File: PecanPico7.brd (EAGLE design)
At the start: 34.2 x 50 mm, 172 parts, among them IC1 Si4464-B1B-FM, IC13 RF6886, IC15 MPU-9250, IC16 PAC1720-1-AIA-TR, IC2 Si4464-B1B-FM, IC3 BME280_BME280, IC4 UBLOX_MAX-6, IC5 STM32F429IIH6, IC6 ALM-GP003, IC7 SPV1040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

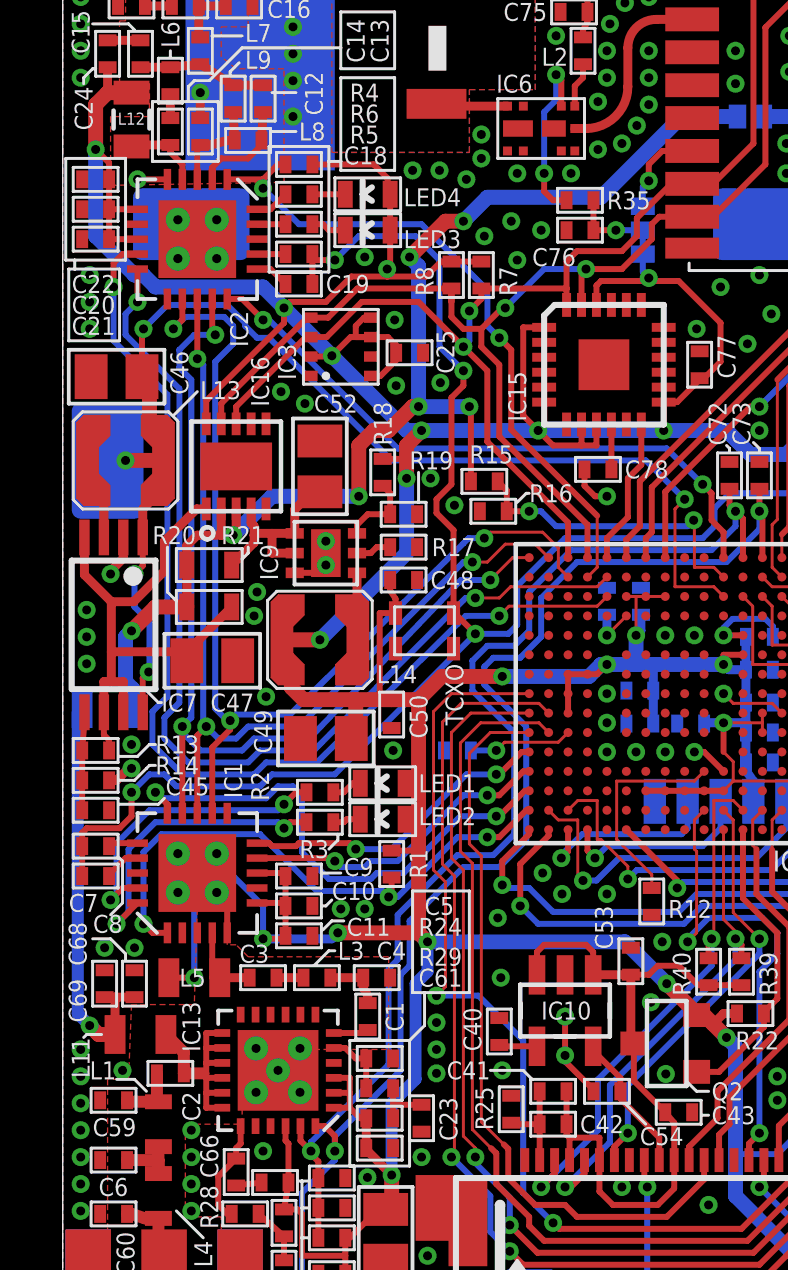
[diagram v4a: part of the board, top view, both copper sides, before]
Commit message: Moved silkscreen
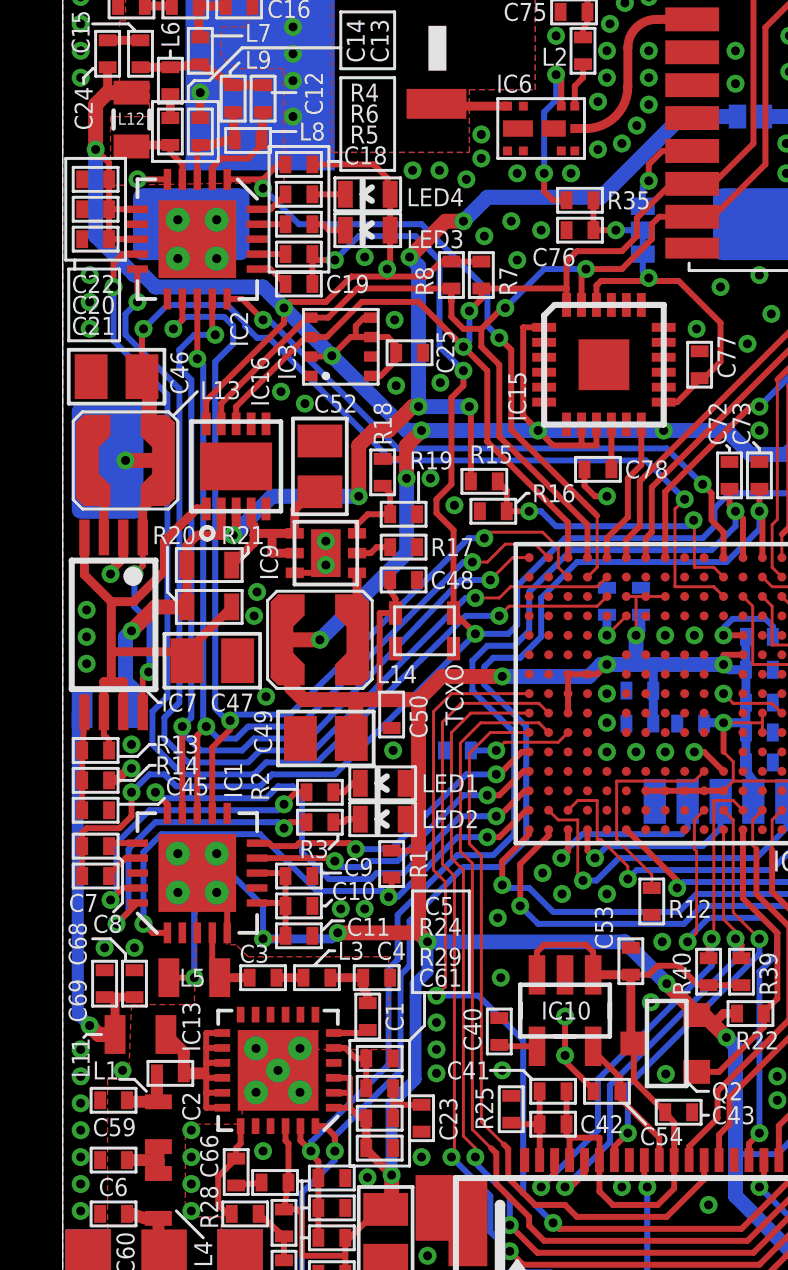
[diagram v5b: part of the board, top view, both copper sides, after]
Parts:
- L1, L4: device sven:0603@1 -> sven2:0603@1
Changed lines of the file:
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@@
 <text x="3.8" y="49.6" size="0.8" layer="38" rot="MR270">RADIO2</text>
 <text x="3" y="0.4" size="0.8" layer="38" rot="MR90">RADIO1</text>
-<text x="1.8" y="40.6" size="0.6" layer="38" rot="MR90">SOLAR GND</text>
-<wire x1="2.4" y1="40" x2="3.2" y2="39.2" width="0.2" layer="38"/>
+<text x="1.8" y="40.7" size="0.6" layer="38" rot="MR90">SOLAR GND</text>
+<wire x1="2.1" y1="40.3" x2="3.2" y2="39.2" width="0.2" layer="38"/>
 <text x="29" y="33.2" size="0.6" layer="38" rot="MR0">SOLAR GND</text>
 <wire x1="24.1" y1="36.4" x2="24.1" y2="35.2" width="0.2" layer="38"/>
@@
 <wire x1="2.1" y1="13.4" x2="1.6" y2="13.9" width="0.1" layer="25"/>
 <wire x1="1.6" y1="13.9" x2="1" y2="13.9" width="0.1" layer="25"/>
-<wire x1="1.6" y1="14.7" x2="2" y2="15.1" width="0.1" layer="25"/>
+<wire x1="1.7" y1="14.8" x2="2" y2="15.1" width="0.1" layer="25"/>
 <wire x1="2" y1="15.1" x2="2" y2="16.5" width="0.1" layer="25"/>
 <wire x1="2" y1="16.5" x2="1.9" y2="16.6" width="0.1" layer="25"/>
 <text x="20.2" y="38.1" size="0.6" layer="38" rot="MR90">GPSBIAS</text>
 <text x="31" y="19.4" size="0.6" layer="38" rot="MR270">RX</text>
-<wire x1="2.4" y1="40" x2="2.1" y2="40.3" width="0.2" layer="26"/>
-<wire x1="2.1" y1="40.3" x2="2.1" y2="40.5" width="0.2" layer="26"/>
+<wire x1="2.1" y1="40.3" x2="2.1" y2="40.5" width="0.2" layer="38"/>
 <wire x1="2.8" y1="19.6" x2="2.9" y2="19.7" width="0.1" layer="21"/>
 <wire x1="2.9" y1="19.7" x2="3.1" y2="19.7" width="0.1" layer="21"/>
@@
 <wire x1="25.9" y1="8.3" x2="26" y2="8.3" width="0.1" layer="25"/>
 <wire x1="26" y1="8.3" x2="26.1" y2="8.4" width="0.1" layer="25"/>
-<wire x1="1.8" y1="9.2" x2="2.4" y2="9.2" width="0.1" layer="25"/>
+<wire x1="1.9" y1="9.2" x2="2.4" y2="9.2" width="0.1" layer="25"/>
 <wire x1="2.4" y1="9.2" x2="2.8" y2="8.8" width="0.1" layer="25"/>
 <wire x1="4.7" y1="3.9" x2="3.8" y2="4.8" width="0.1" layer="25"/>
 <text x="5.3" y="21.9" size="1.1" layer="38" rot="MR90">Pecan Pico 7
 rev1.0</text>
-<text x="4.9" y="8.8" size="1" layer="38" rot="MR90">Dec 2015</text>
+<text x="4.9" y="7.7" size="1" layer="38" rot="MR90">Dec 2015</text>
 <wire x1="0.7" y1="10.6" x2="0.8" y2="10.7" width="0.1" layer="25"/>
 <wire x1="0.8" y1="10.7" x2="1.3" y2="10.7" width="0.1" layer="25"/>
@@
 </element>
 <element name="LED1" library="PecanPico6" package="LED-0603" value="yellow" x="10.7" y="19.1" smashed="yes" rot="R90">
-<attribute name="NAME" x="11.9" y="18.8" size="0.6" layer="25"/>
+<attribute name="NAME" x="12" y="18.8" size="0.6" layer="25"/>
 <attribute name="VALUE" x="11.8" y="20.5" size="0.6" layer="27" rot="R180"/>
 </element>
 <element name="LED2" library="PecanPico6" package="LED-0603" value="blue" x="10.7" y="17.9" smashed="yes" rot="R90">
-<attribute name="NAME" x="11.9" y="17.7" size="0.6" layer="25"/>
+<attribute name="NAME" x="12" y="17.6" size="0.6" layer="25"/>
 <attribute name="VALUE" x="11.8" y="19.3" size="0.6" layer="27" rot="R180"/>
 </element>
@@
 </element>
 <element name="LED3" library="PecanPico6" package="LED-0603" value="yellow" x="10.2" y="37.6" smashed="yes" rot="R90">
-<attribute name="NAME" x="11.4" y="37" size="0.6" layer="25"/>
+<attribute name="NAME" x="11.5" y="37" size="0.6" layer="25"/>
 <attribute name="VALUE" x="11.3" y="39" size="0.6" layer="27" rot="R180"/>
 </element>
 <element name="LED4" library="PecanPico6" package="LED-0603" value="blue" x="10.2" y="38.8" smashed="yes" rot="R90">
-<attribute name="NAME" x="11.4" y="38.4" size="0.6" layer="25"/>
+<attribute name="NAME" x="11.5" y="38.4" size="0.6" layer="25"/>
 <attribute name="VALUE" x="11.3" y="40.2" size="0.6" layer="27" rot="R180"/>
 </element>
@@
 </element>
 <element name="R16" library="PecanPico6" package="0402" value="10k" x="14.4" y="28.2" smashed="yes">
-<attribute name="NAME" x="15.6" y="28.5" size="0.6" layer="25"/>
+<attribute name="NAME" x="15.7" y="28.5" size="0.6" layer="25"/>
 <attribute name="VALUE" x="13.7" y="27" size="0.6" layer="27"/>
 </element>
@@
 </element>
 <element name="R17" library="PecanPico6" package="0402" value="47k" x="11.4" y="27" smashed="yes" rot="R180">
-<attribute name="NAME" x="13.8" y="27.3" size="0.6" layer="25" rot="R180"/>
+<attribute name="NAME" x="12.3" y="26.7" size="0.6" layer="25"/>
 <attribute name="VALUE" x="12.1" y="28.2" size="0.6" layer="27" rot="R180"/>
 </element>
@@
 </element>
 <element name="C64" library="PecanPico6" package="0402" value="1uF" x="8.4" y="1.3" smashed="yes" rot="R90">
-<attribute name="NAME" x="10.25" y="6.3" size="0.6" layer="26" rot="MR270"/>
+<attribute name="NAME" x="9.65" y="4.8" size="0.6" layer="26" rot="MR90"/>
 <attribute name="VALUE" x="9.6" y="0.6" size="0.6" layer="27" rot="R90"/>
 </element>
 <element name="R26" library="PecanPico6" package="0402" value="390R" x="9" y="3.9" smashed="yes">
-<attribute name="NAME" x="9.85" y="3.25" size="0.6" layer="26" rot="MR180"/>
+<attribute name="NAME" x="11.4" y="2.65" size="0.6" layer="26" rot="MR0"/>
 <attribute name="VALUE" x="8.3" y="2.7" size="0.6" layer="27"/>
 </element>
 <element name="R27" library="PecanPico6" package="0402" value="390R" x="9" y="2.7" smashed="yes">
-<attribute name="NAME" x="9.85" y="4.35" size="0.6" layer="26" rot="MR180"/>
+<attribute name="NAME" x="11.4" y="3.75" size="0.6" layer="26" rot="MR0"/>
 <attribute name="VALUE" x="8.3" y="1.5" size="0.6" layer="27"/>
 </element>
 <element name="C65" library="PecanPico6" package="0402" value="1uF" x="7.1" y="5.75" smashed="yes">
-<attribute name="NAME" x="7.95" y="1.25" size="0.6" layer="26" rot="MR180"/>
+<attribute name="NAME" x="9.5" y="0.65" size="0.6" layer="26" rot="MR0"/>
 <attribute name="VALUE" x="6.4" y="4.55" size="0.6" layer="27"/>
 </element>
@@
 </element>
 <element name="C67" library="PecanPico6" package="0402" value="1uF" x="7.4" y="2.7" smashed="yes" rot="R90">
-<attribute name="NAME" x="9.15" y="5.15" size="0.6" layer="26" rot="MR270"/>
+<attribute name="NAME" x="8.55" y="3.6" size="0.6" layer="26" rot="MR90"/>
 <attribute name="VALUE" x="8.6" y="2" size="0.6" layer="27" rot="R90"/>
 </element>
@@
 <attribute name="VALUE" x="22.6" y="21" size="0.6" layer="28" rot="MR180"/>
 </element>
-<element name="L1" library="sven" package="0603@1" value="68nH" x="3.2" y="7.7" smashed="yes" rot="R270">
-<attribute name="NAME" x="0.9" y="9.2" size="0.6" layer="25"/>
+<element name="L1" library="sven2" package="0603@1" value="68nH" x="3.2" y="7.7" smashed="yes" rot="R270">
+<attribute name="NAME" x="1" y="9.2" size="0.6" layer="25"/>
 <attribute name="VALUE" x="2" y="8.7" size="0.2" layer="27" rot="R270"/>
 </element>
-<element name="L4" library="sven" package="0603@1" value="68nH" x="3.2" y="5.3" smashed="yes" rot="R270">
+<element name="L4" library="sven2" package="0603@1" value="68nH" x="3.2" y="5.3" smashed="yes" rot="R270">
 <attribute name="NAME" x="4.4" y="3.8" size="0.6" layer="25" rot="R270"/>
 <attribute name="VALUE" x="2" y="6.3" size="0.2" layer="27" rot="R270"/>
@@
 </element>
 <element name="R30" library="PecanPico6" package="0402" value="RES-0402" x="7.4" y="4.4" smashed="yes" rot="R90">
-<attribute name="NAME" x="9.15" y="3.25" size="0.6" layer="26" rot="MR270"/>
+<attribute name="NAME" x="8.55" y="1.7" size="0.6" layer="26" rot="MR90"/>
 <attribute name="VALUE" x="8.6" y="3.7" size="0.6" layer="27" rot="R90"/>
 </element>

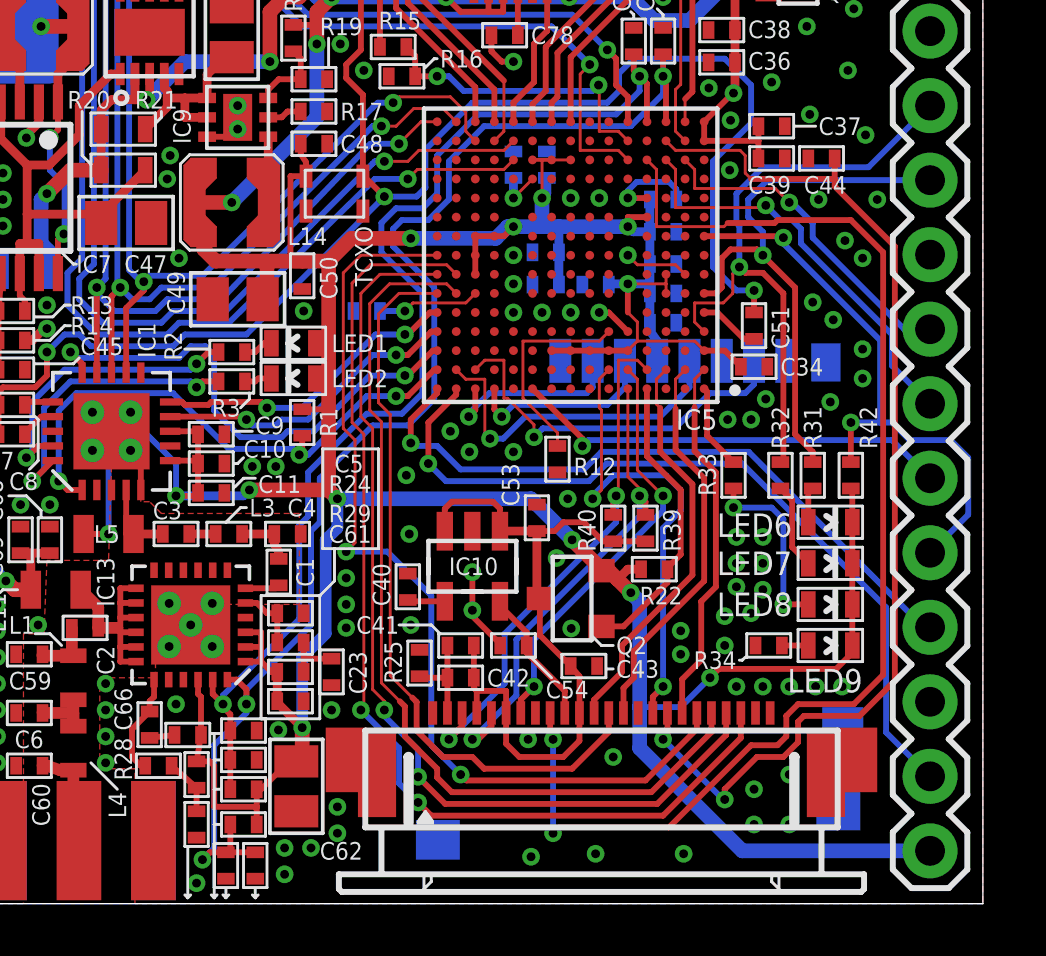
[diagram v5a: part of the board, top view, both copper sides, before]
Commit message: Moved Silkscreen, improved GND-connections
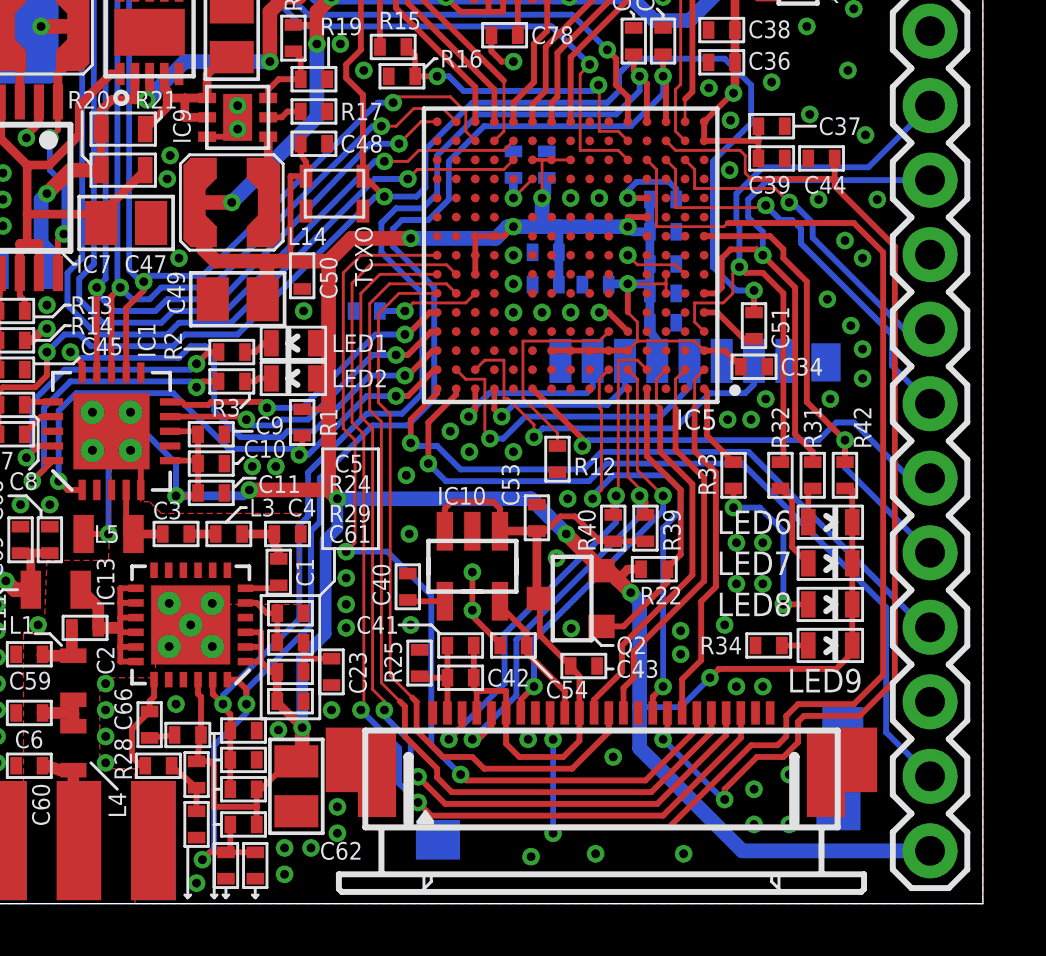
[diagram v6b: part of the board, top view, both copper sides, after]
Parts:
- moved R42 0.20 mm to (29.5, 14.6)
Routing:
- net NRST: track 20.0 -> 16.0 mm, vias 2 -> 1
- net GND: vias 189 -> 182
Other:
- board text added: "I2C SCL I2C SDA"
- board text removed: "I2C SDA I2C SCL"

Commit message: Adjusted values
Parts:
- C12: value 4.7pF -> 2.7pF
- C13: value 4.7pF -> 5.1pF
- C14: value 470pF -> 9.1pF
- C15: value 18pF -> 15pF
- C16: value 22pF -> 12pF
- C17, C59: value 22pF -> (none)
- C24: value 470pF -> 100pF
- C74: value CAP-0402 -> 100nF
- C75: value CAP-0402 -> 47pF
- C76: value CAP-0402 -> 330pF
- L1: value 68nH -> 56nH
- L10: value 68nH -> 36nH
- L11, L5: value (none) -> 470nH
- L12: value (none) -> 220nH
- L15: value IND-0402 -> 22nH
- L2: value IND-0402 -> 1.8nH
- L6: value 56nH -> 33nH
- L7: value 68nH -> 30nH
- R11, R31: value 3.3k -> 2.2k
- R15: value 10k -> 22k
- R17: value 47k -> 0R
- R18: value 720k -> 680k
- R19: value 180k -> 210k
- R29, R30: value RES-0402 -> (none)
- R35: value RES-0402 -> 4.7k
- R36: value RES-0402 -> 10k
- TCXO: value TG-5006CJ-19H -> KT2016K2BCW18ZAS

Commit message: Renamed components
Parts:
- IC1: value Si4464-B1B-FM -> Si4060-B1B-FM
- IC4: value UBLOX_MAX-6 -> uBlox MAX7/8
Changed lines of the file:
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@@
 </autorouter>
 <elements>
-<element name="IC1" library="PecanPico6" package="QFN-20" value="Si4464-B1B-FM" x="4.5" y="16.1" smashed="yes" rot="R90">
+<element name="IC1" library="PecanPico6" package="QFN-20" value="Si4060-B1B-FM" x="4.5" y="16.1" smashed="yes" rot="R90">
 <attribute name="VALUE" x="7.7" y="14.4" size="0.6" layer="27" rot="R90"/>
 <attribute name="NAME" x="6" y="18.6" size="0.6" layer="25" rot="R90"/>
@@
 <attribute name="VALUE" x="12.3" y="34.7" size="0.6" layer="27" rot="R180"/>
 </element>
-<element name="IC4" library="PecanPico6" package="UBLOX_MAX-6" value="UBLOX_MAX-6" x="25.6" y="41.4"/>
+<element name="IC4" library="PecanPico6" package="UBLOX_MAX-6" value="uBlox MAX7/8" x="25.6" y="41.4"/>
 <element name="R9" library="PecanPico6" package="0402" value="47k" x="32.6" y="46.2" smashed="yes" rot="R180">
 <attribute name="NAME" x="33.4" y="46.7" size="0.6" layer="25" rot="R270"/>
